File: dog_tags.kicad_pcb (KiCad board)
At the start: 4 copper layers, 49.4 x 28.1 mm, 44 parts

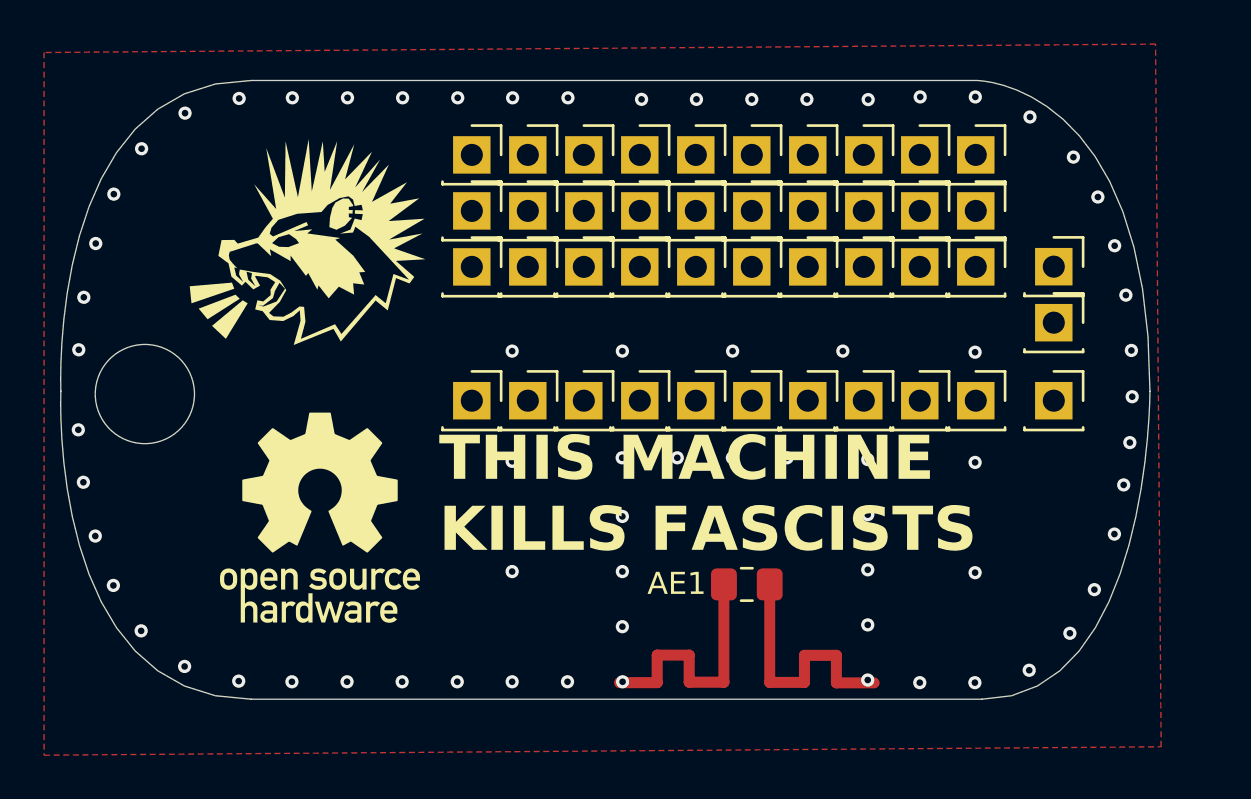
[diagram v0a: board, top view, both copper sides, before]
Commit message: change graphics and text to CfN
Signed-off-by: Lucy Mielke <user@domain.tld>
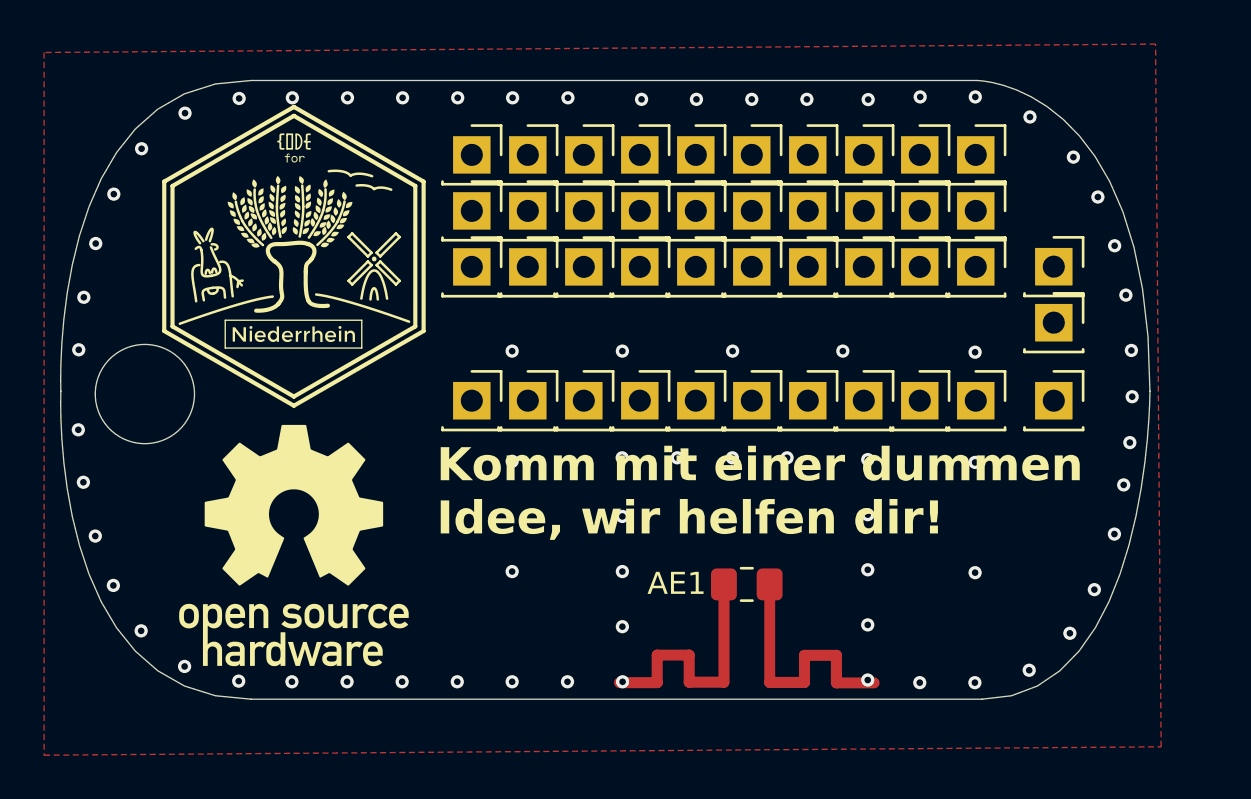
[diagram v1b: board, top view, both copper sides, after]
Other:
- board text added: "Komm mit einer dummen Idee, wir helfen dir!"
- board text added: "https://codeforniederrhein.de"
- board text removed: "THIS MACHINE KILLS FASCISTS"
- board text removed: "engineering.redlucy404.de"
